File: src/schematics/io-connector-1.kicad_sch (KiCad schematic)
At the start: 1 part, among them J13 DDR4_SODIMM_Board

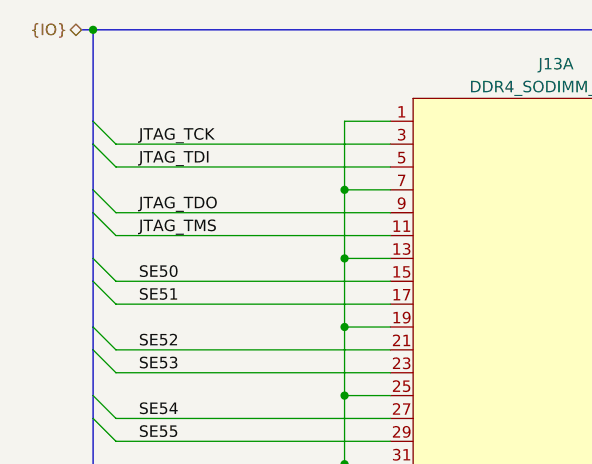
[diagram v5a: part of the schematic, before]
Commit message: fanout the io connector
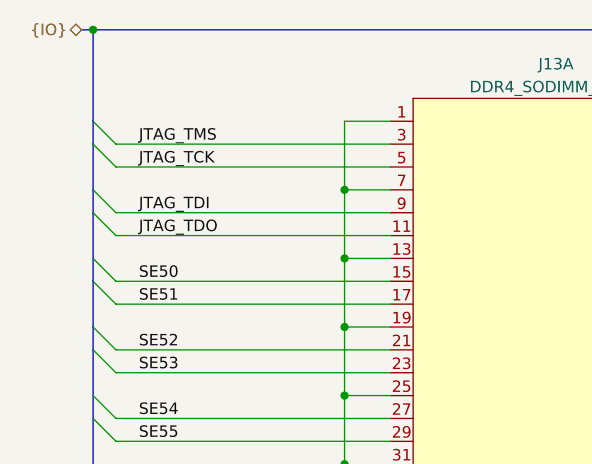
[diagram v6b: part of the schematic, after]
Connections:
- net JTAG_TCK: now also J13.5; no longer J13.3
- net JTAG_TDI: now also J13.9; no longer J13.5
- net JTAG_TDO: now also J13.11; no longer J13.9
- net JTAG_TMS: now also J13.3; no longer J13.11
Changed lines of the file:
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@@
 	)
 	(label "JTAG_TCK"
-		(at 45.72 53.34 0)
+		(at 45.72 55.88 0)
 		(effects
 			(font
@@
 	)
 	(label "JTAG_TMS"
-		(at 45.72 63.5 0)
+		(at 45.72 53.34 0)
 		(effects
 			(font
@@
 	)
 	(label "JTAG_TDO"
-		(at 45.72 60.96 0)
+		(at 45.72 63.5 0)
 		(effects
 			(font
@@
 	)
 	(label "JTAG_TDI"
-		(at 45.72 55.88 0)
-		(effects
-			(font
+		(at 45.72 60.96 0)
+		(effects
+			(font

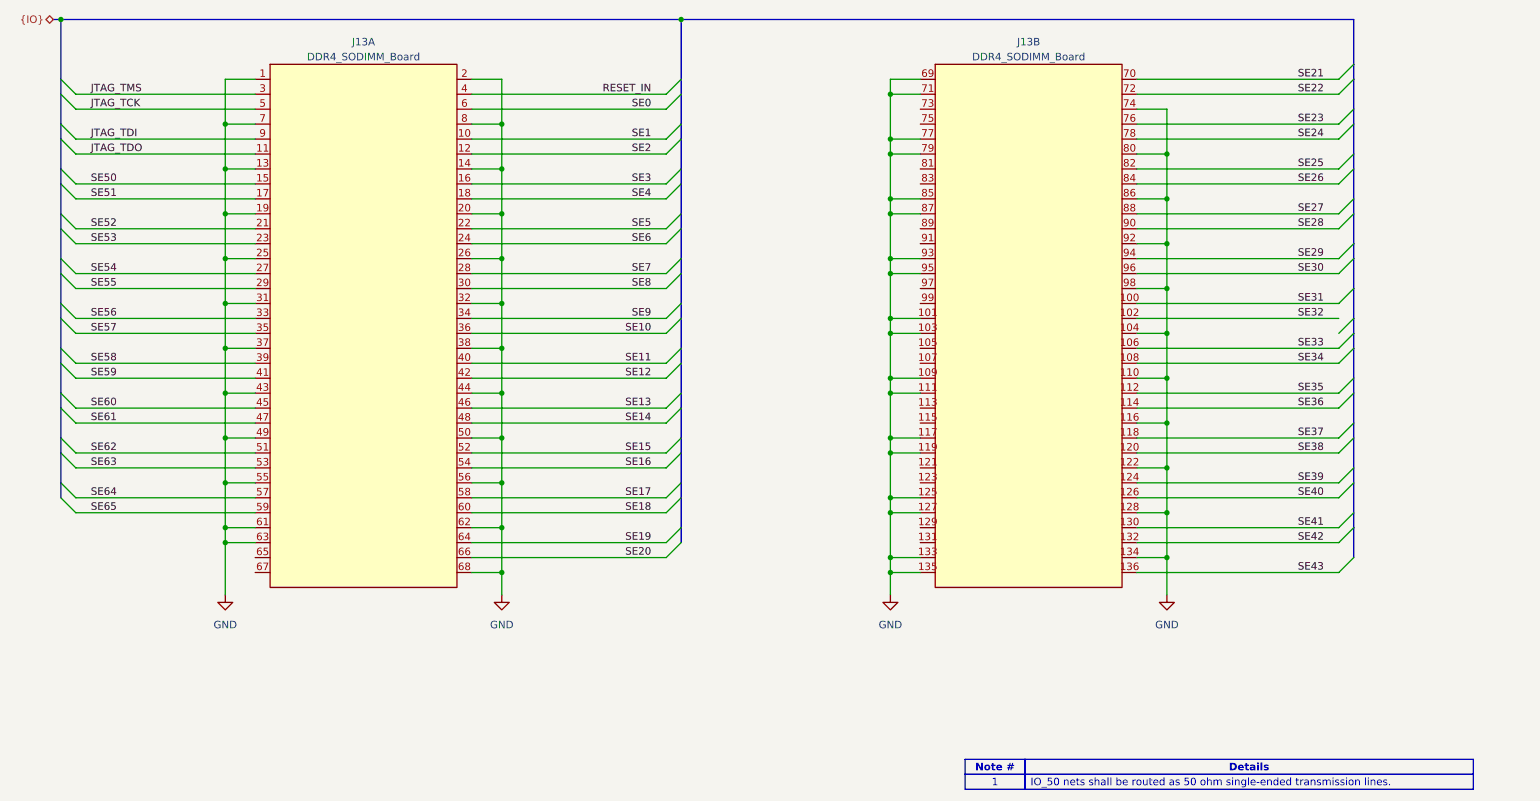
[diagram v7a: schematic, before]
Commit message: Fix ERC after routing completion
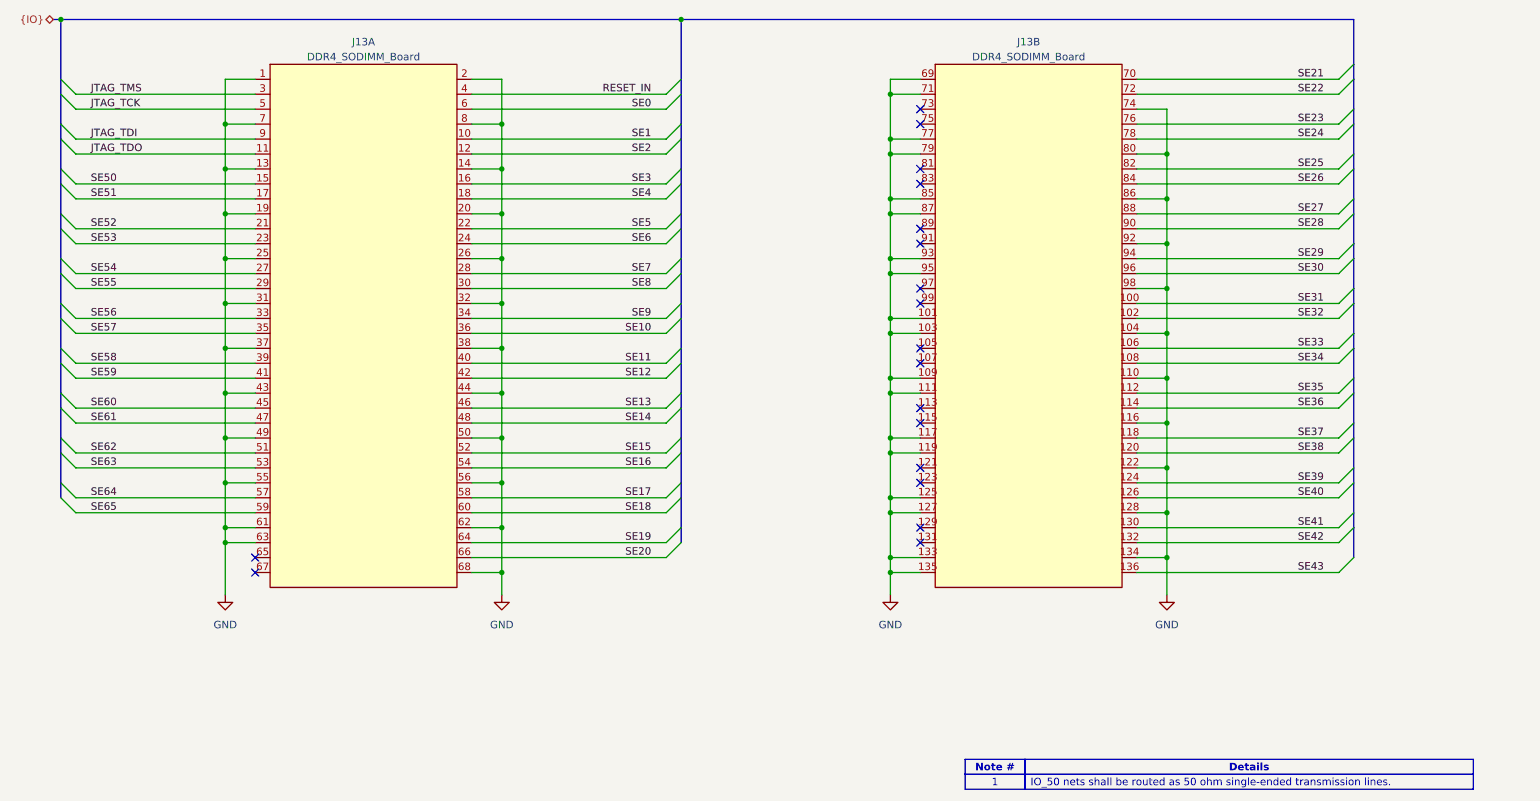
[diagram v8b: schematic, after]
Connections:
- no-connect marks 0 -> 18
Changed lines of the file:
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@@
 		(color 0 0 0 0)
+	)
+	(no_connect
+		(at 186.69 86.36)
+	)
+	(no_connect
+		(at 186.69 76.2)
+	)
+	(no_connect
+		(at 186.69 116.84)
+	)
+	(no_connect
+		(at 186.69 106.68)
+	)
+	(no_connect
+		(at 186.69 99.06)
+	)
+	(no_connect
+		(at 186.69 66.04)
+	)
+	(no_connect
+		(at 186.69 78.74)
+	)
+	(no_connect
+		(at 186.69 55.88)
+	)
+	(no_connect
+		(at 186.69 88.9)
+	)
+	(no_connect
+		(at 186.69 119.38)
+	)
+	(no_connect
+		(at 186.69 58.42)
+	)
+	(no_connect
+		(at 73.66 132.08)
+	)
+	(no_connect
+		(at 186.69 68.58)
+	)
+	(no_connect
+		(at 186.69 109.22)
+	)
+	(no_connect
+		(at 186.69 127)
+	)
+	(no_connect
+		(at 186.69 96.52)
+	)
+	(no_connect
+		(at 186.69 129.54)
+	)
+	(no_connect
+		(at 73.66 134.62)
 	)
 	(bus_entry
@@
 	)
 	(bus_entry
-		(at 260.35 91.44)
+		(at 260.35 88.9)
 		(size -2.54 2.54)
 		(stroke
@@
 	(bus
 		(pts
-			(xy 260.35 86.36) (xy 260.35 91.44)
+			(xy 260.35 86.36) (xy 260.35 88.9)
 		)
 		(stroke
@@
 		)
 	)
+	(bus
+		(pts
+			(xy 260.35 88.9) (xy 260.35 93.98)
+		)
+		(stroke
+			(width 0)
+			(type default)
+		)
+	)
 	(wire
 		(pts
@@
 		)
 		(stroke
-			(width 0)
-			(type default)
-		)
-	)
-	(bus
-		(pts
-			(xy 260.35 91.44) (xy 260.35 93.98)
-		)
-		(stroke
